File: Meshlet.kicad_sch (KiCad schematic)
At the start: 102 parts, among them J11 GPIO Exp., J12 GPS Header, J13 Thermistor Pins, J14 Ext. Notif. Header, J2 User Btn Header, J3 Batt. Header (Picoblade 1.25), J4 Batt. Header (JST-PH 2.0), J5 USB_C_Receptacle_USB2.0_16P, J6 STEMMA QT I2C, J7 Ext. Power Header, J9 Ext. Power Header, Q1 AO3400A, SW2 BOOTSEL, U1 XC6206PxxxMR, U11 INA3221, U2 USBLC6-2SC6, U3 XC6206PxxxMR, U4 RP2350_60QFN, U5 Wio-SX1262, U6 BQ25185, U7 BME280, U8 W25Q32JVZP, U9 XC6206PxxxMR, Y1 12.000MHz

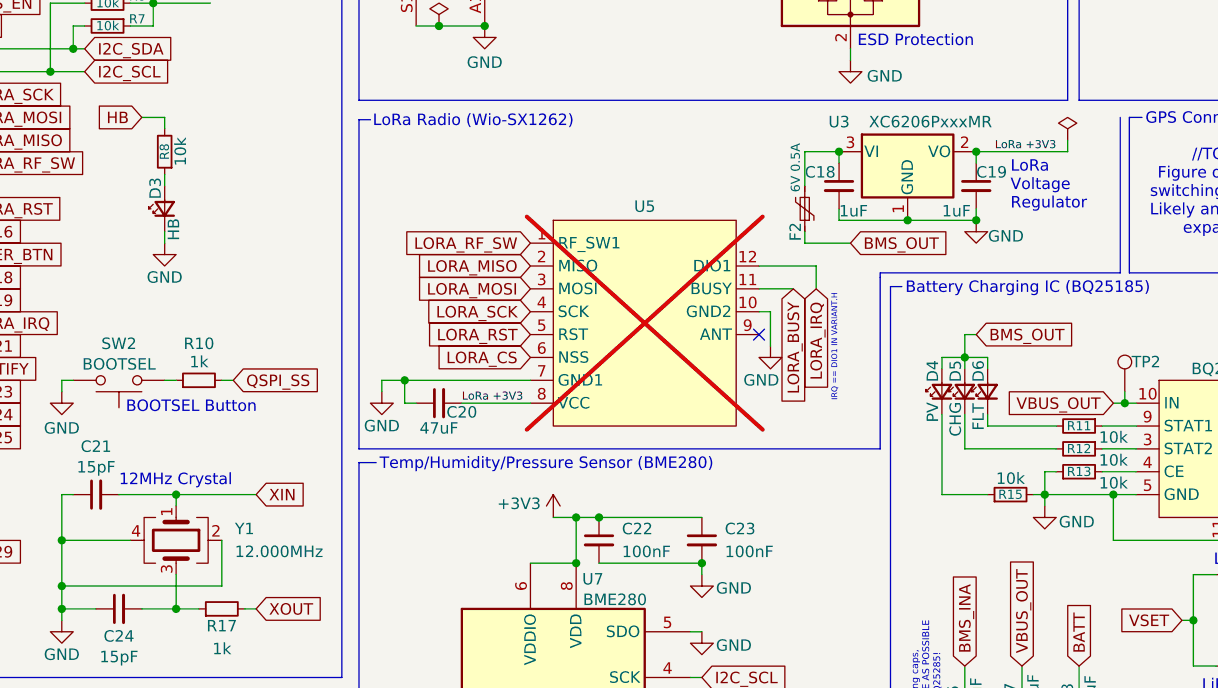
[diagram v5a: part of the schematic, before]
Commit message: Trace tuning, silkscreen touch-ups, BOM touch-ups
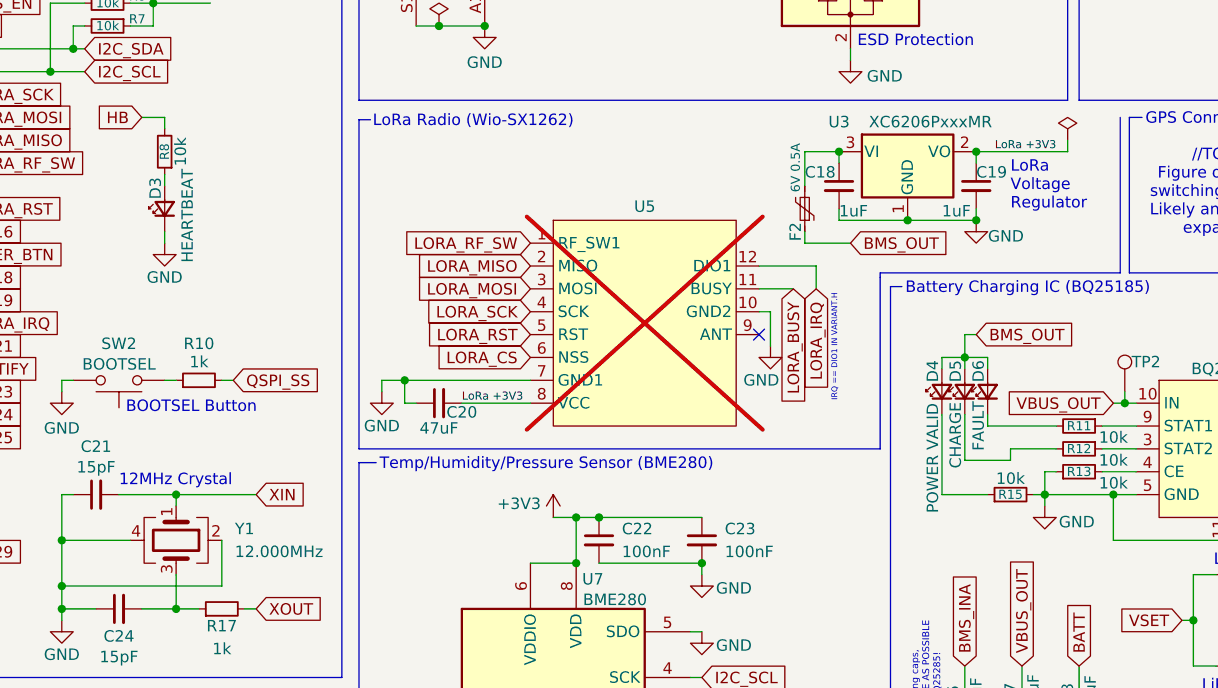
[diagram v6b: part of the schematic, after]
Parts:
- C26, C27, C28: LCSC (none) -> C105226
- D3: value HB -> HEARTBEAT
- D4: value PV -> POWER VALID
- D5: value CHG -> CHARGE
- D6: value FLT -> FAULT
- J6: value STEMMA QT I2C -> I2C Header; LCSC C50137 -> (none)
- J9: LCSC C27910 -> (none)
- Q1: LCSC (none) -> C20917
- R14, R28: LCSC (none) -> C25744
- R16: LCSC (none) -> C25754
- R18: LCSC (none) -> C25905
- R19: LCSC (none) -> C25102
- R20: LCSC (none) -> C25126
- R21: LCSC (none) -> C25862
- R25: LCSC (none) -> C25117
- U6: LCSC (none) -> C19725033
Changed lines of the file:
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@@
 	(wire
 		(pts
-			(xy 217.17 114.3) (xy 227.33 114.3)
+			(xy 217.17 115.57) (xy 222.25 115.57)
 		)
 		(stroke
@@
 	(wire
 		(pts
-			(xy 217.17 114.3) (xy 217.17 110.49)
+			(xy 217.17 115.57) (xy 217.17 110.49)
 		)
 		(stroke
@@
 	(wire
 		(pts
+			(xy 222.25 114.3) (xy 227.33 114.3)
+		)
+		(stroke
+			(width 0)
+			(type default)
+		)
+	)
+	(wire
+		(pts
 			(xy 96.52 166.37) (xy 99.06 166.37)
 		)
@@
 	(wire
 		(pts
+			(xy 222.25 115.57) (xy 222.25 114.3)
+		)
+		(stroke
+			(width 0)
+			(type default)
+		)
+	)
+	(wire
+		(pts
 			(xy 179.07 44.45) (xy 179.07 41.91)
 		)
@@
 			)
 		)
-		(property "Value" "STEMMA QT I2C"
+		(property "Value" "I2C Header"
 			(at 257.81 53.34 0)
 			(effects
@@
 			)
 		)
-		(property "LCSC" "C50137"
+		(property "LCSC" ""
 			(at 257.81 44.45 0)
 			(effects
@@
 			)
 		)
-		(property "Value" "PV"
-			(at 213.614 110.236 0)
+		(property "Value" "POWER VALID"
+			(at 213.614 115.316 0)
 			(effects
 				(font
@@
 			)
 		)
+		(property "LCSC" "C25754"
+			(at 247.65 128.27 90)
+			(effects
+				(font
+					(size 1.27 1.27)
+				)
+				(hide yes)
+			)
+		)
 		(pin "1"
 		)
@@
 			)
 		)
-		(property "Value" "CHG"
-			(at 216.154 110.998 0)
+		(property "Value" "CHARGE"
+			(at 216.154 112.776 0)
 			(effects
 				(font
@@
 			)
 		)
+		(property "LCSC" "C25117"
+			(at 39.37 176.53 90)
+			(effects
+				(font
+					(size 1.27 1.27)
+				)
+				(hide yes)
+			)
+		)
 		(pin "2"
 		)
@@
 			)
 		)
-		(property "Value" "HB"
-			(at 129.286 89.916 0)
+		(property "Value" "HEARTBEAT"
+			(at 130.81 88.392 0)
 			(effects
 				(font
@@
 			)
 		)
+		(property "LCSC" "C25126"
+			(at 273.05 143.51 90)
+			(effects
+				(font
+					(size 1.27 1.27)
+				)
+				(hide yes)
+			)
+		)
 		(pin "1"
 		)
@@
 			)
 		)
-		(property "LCSC" "C27910"
+		(property "LCSC" ""
 			(at 234.95 44.45 0)
 			(effects
@@
 			)
 		)
+		(property "LCSC" "C25862"
+			(at 278.13 143.51 90)
+			(effects
+				(font
+					(size 1.27 1.27)
+				)
+				(hide yes)
+			)
+		)
 		(pin "1"
 		)
@@
 			)
 		)
+		(property "LCSC" "C105226"
+			(at 229.87 144.78 90)
+			(effects
+				(font
+					(size 1.27 1.27)
+				)
+				(hide yes)
+			)
+		)
 		(pin "2"
 		)
@@
 			)
 		)
-		(property "Value" "FLT"
-			(at 218.694 110.744 0)
+		(property "Value" "FAULT"
+			(at 218.694 111.76 0)
 			(effects
 				(font
@@
 			)
 		)
+		(property "LCSC" "C25102"
+			(at 267.97 143.51 90)
+			(effects
+				(font
+					(size 1.27 1.27)
+				)
+				(hide yes)
+			)
+		)
 		(pin "1"
 		)
@@
 			)
 		)
+		(property "LCSC" "C19725033"
+			(at 246.38 114.3 0)
+			(effects
+				(font
+					(size 1.27 1.27)
+				)
+				(hide yes)
+			)
+		)
 		(pin "9"
 		)
@@
 			)
 		)
+		(property "LCSC" "C20917"
+			(at 162.56 182.88 0)
+			(effects
+				(font
+					(size 1.27 1.27)
+				)
+				(hide yes)
+			)
+		)
 		(pin "1"
 		)
@@
 			)
 		)
+		(property "LCSC" "C105226"
+			(at 217.17 144.78 90)
+			(effects
+				(font
+					(size 1.27 1.27)
+				)
+				(hide yes)
+			)
+		)
 		(pin "2"
 		)
@@
 			)
 		)
+		(property "LCSC" "C25905"
+			(at 247.65 138.43 90)
+			(effects
+				(font
+					(size 1.27 1.27)
+				)
+				(hide yes)
+			)
+		)
 		(pin "1"
 		)
@@
 			)
 		)
+		(property "LCSC" "C25744"
+			(at 269.24 118.11 90)
+			(effects
+				(font
+					(size 1.27 1.27)
+				)
+				(hide yes)
+			)
+		)
 		(pin "1"
 		)
@@
 			)
 		)
+		(property "LCSC" "C25744"
+			(at 39.37 186.69 90)
+			(effects
+				(font
+					(size 1.27 1.27)
+				)
+				(hide yes)
+			)
+		)
 		(pin "2"
 		)
@@
 			(effects
 				(font
+					(size 1.27 1.27)
+				)
+				(hide yes)
+			)
+		)
+		(property "LCSC" "C105226"
+			(at 223.52 144.78 90)
+			(effects
+				(font

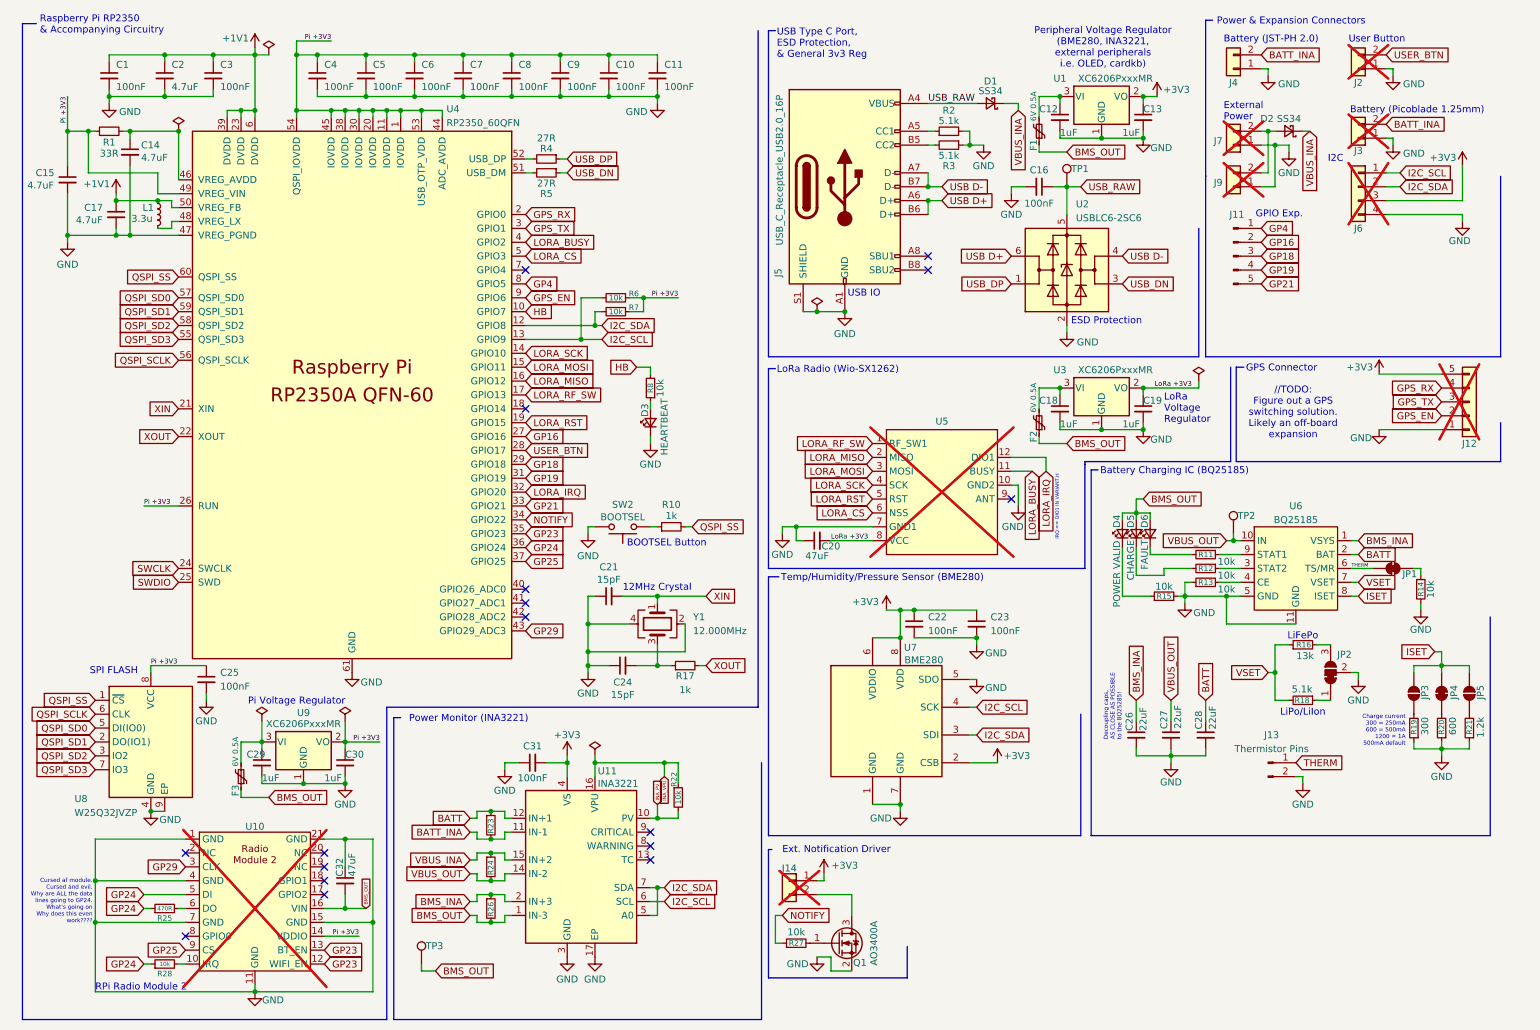
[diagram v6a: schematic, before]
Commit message: Fix text sizes for production, fix batt chem label
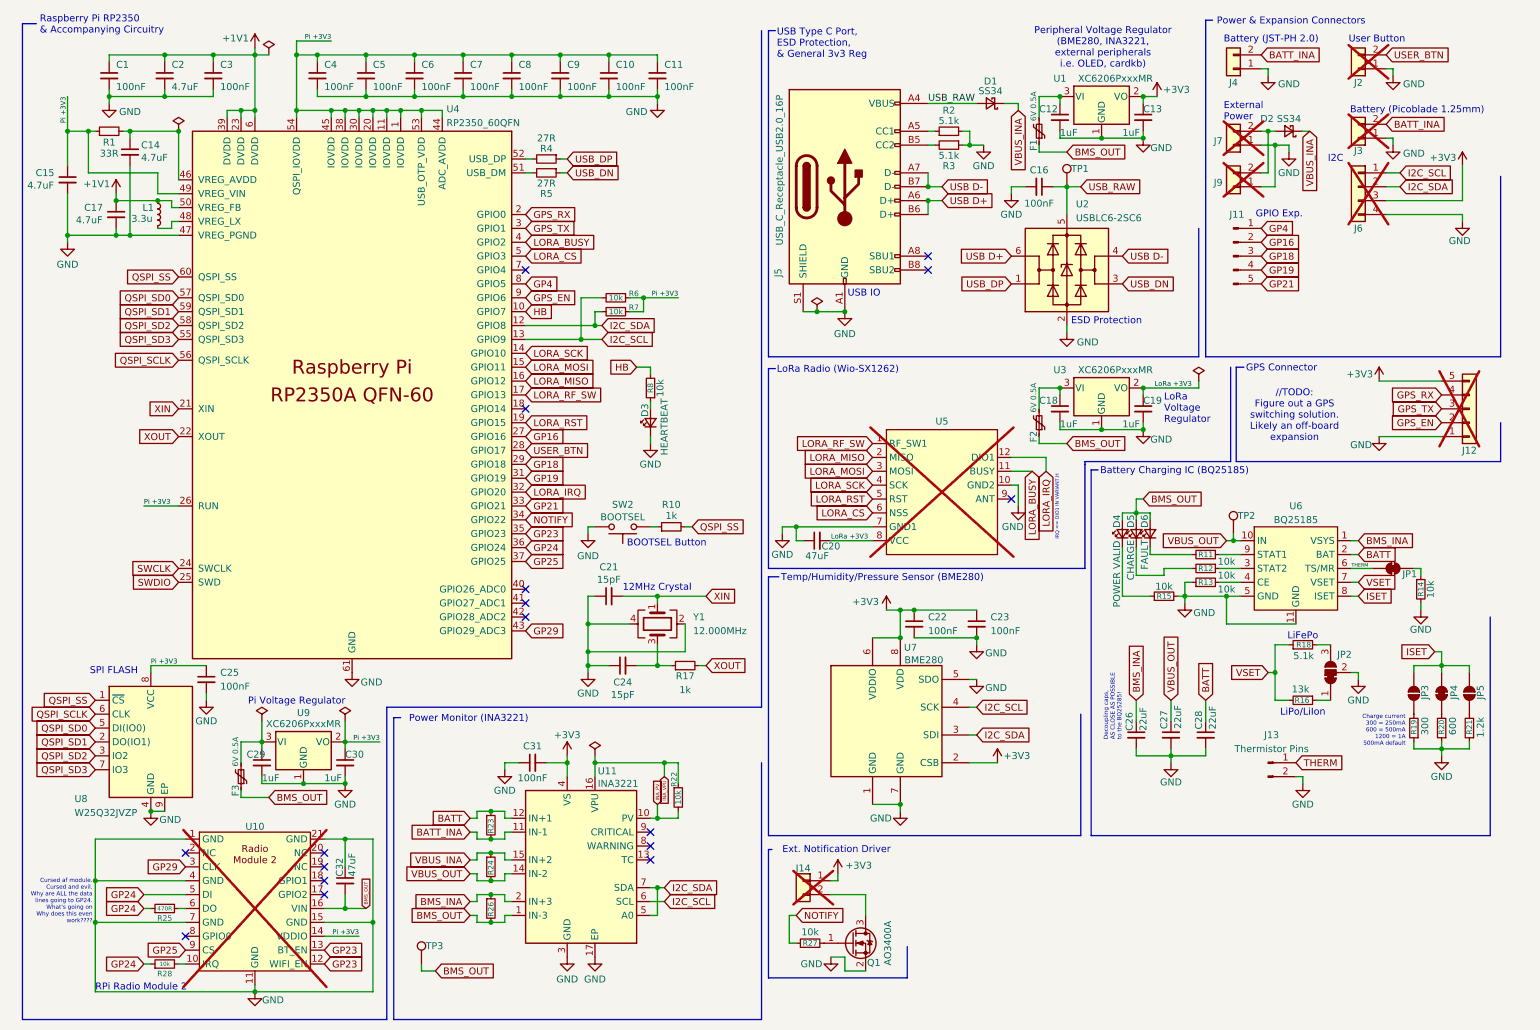
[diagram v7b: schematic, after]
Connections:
- net VSET: now also R16.2, R18.1; no longer R16.1, R18.2
- net at JP2.3 (B): now also R18.2; no longer R16.2
- net at JP2.1 (A): now also R16.1; no longer R18.1
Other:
- moved on the sheet: J12, J14, Q1, R16, R18, R27

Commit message: ibom updates
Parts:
- D3: value HEARTBEAT -> HEARTBEAT (Red)
- D4: value POWER VALID -> POWER VALID (Grn)
- D5: value CHARGE -> CHARGE (Blu)
- D6: value FAULT -> FAULT (Red)
- F1, F2, F3: value 6V 0.5A -> 6V 0.5A 0603
- J13: value Thermistor Pins -> 10k Thermistor
- JP3: value SolderJumper_2_Open -> 250mA Charge
- JP4: value SolderJumper_2_Bridged -> 500mA Charge
- JP5: value SolderJumper_2_Open -> 1A Charge
- SW2: value BOOTSEL -> BOOTSEL Sw
- U10: value ~ -> RPi RM2
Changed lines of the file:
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@@
 			)
 		)
-		(property "Value" "Thermistor Pins"
+		(property "Value" "10k Thermistor"
 			(at 241.935 147.32 0)
 			(effects
@@
 			)
 		)
-		(property "Value" "POWER VALID"
+		(property "Value" "POWER VALID (Grn)"
 			(at 213.614 115.316 0)
 			(effects
@@
 			)
 		)
-		(property "Value" "CHARGE"
+		(property "Value" "CHARGE (Blu)"
 			(at 216.154 112.776 0)
 			(effects
@@
 			)
 		)
-		(property "Value" "SolderJumper_2_Bridged"
+		(property "Value" "500mA Charge"
 			(at 275.59 138.4299 90)
 			(effects
@@
 			)
 		)
-		(property "Value" "6V 0.5A"
+		(property "Value" "6V 0.5A 0603"
 			(at 198.374 29.718 90)
 			(effects
@@
 			)
 		)
-		(property "Value" "HEARTBEAT"
+		(property "Value" "HEARTBEAT (Red)"
 			(at 130.81 88.392 0)
 			(effects
@@
 			)
 		)
-		(property "Value" "6V 0.5A"
+		(property "Value" "6V 0.5A 0603"
 			(at 52.324 147.828 90)
 			(effects
@@
 			)
 		)
-		(property "Value" "6V 0.5A"
+		(property "Value" "6V 0.5A 0603"
 			(at 198.374 83.058 90)
 			(effects
@@
 			)
 		)
-		(property "Value" "BOOTSEL"
+		(property "Value" "BOOTSEL Sw"
 			(at 123.19 104.902 0)
 			(effects
@@
 			)
 		)
-		(property "Value" "FAULT"
+		(property "Value" "FAULT (Red)"
 			(at 218.694 111.76 0)
 			(effects
@@
 			)
 		)
-		(property "Value" "SolderJumper_2_Open"
+		(property "Value" "250mA Charge"
 			(at 270.51 138.4299 90)
 			(effects
@@
 			)
 		)
-		(property "Value" "~"
+		(property "Value" "RPi RM2"
 			(at 55.88 161.29 0)
 			(effects
@@
 			)
 		)
-		(property "Value" "SolderJumper_2_Open"
+		(property "Value" "1A Charge"
 			(at 280.67 138.4299 90)
 			(effects
